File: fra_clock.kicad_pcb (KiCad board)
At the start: 2 copper layers, 210 x 297 mm, 425 parts, among them J1 USB_C, J101 SPK_TOP, J102 SPK_BOT, Q1 MMBT3904, Q2 MMBT3904, Q3 2N7002, U1 AP2112K-3.3, U101 MAX98357A, U102 MAX98357A, U2 USBLC6-2SC6, U3 ESP32-WROOM-32E, U5 CH340C, U6 74AHCT125

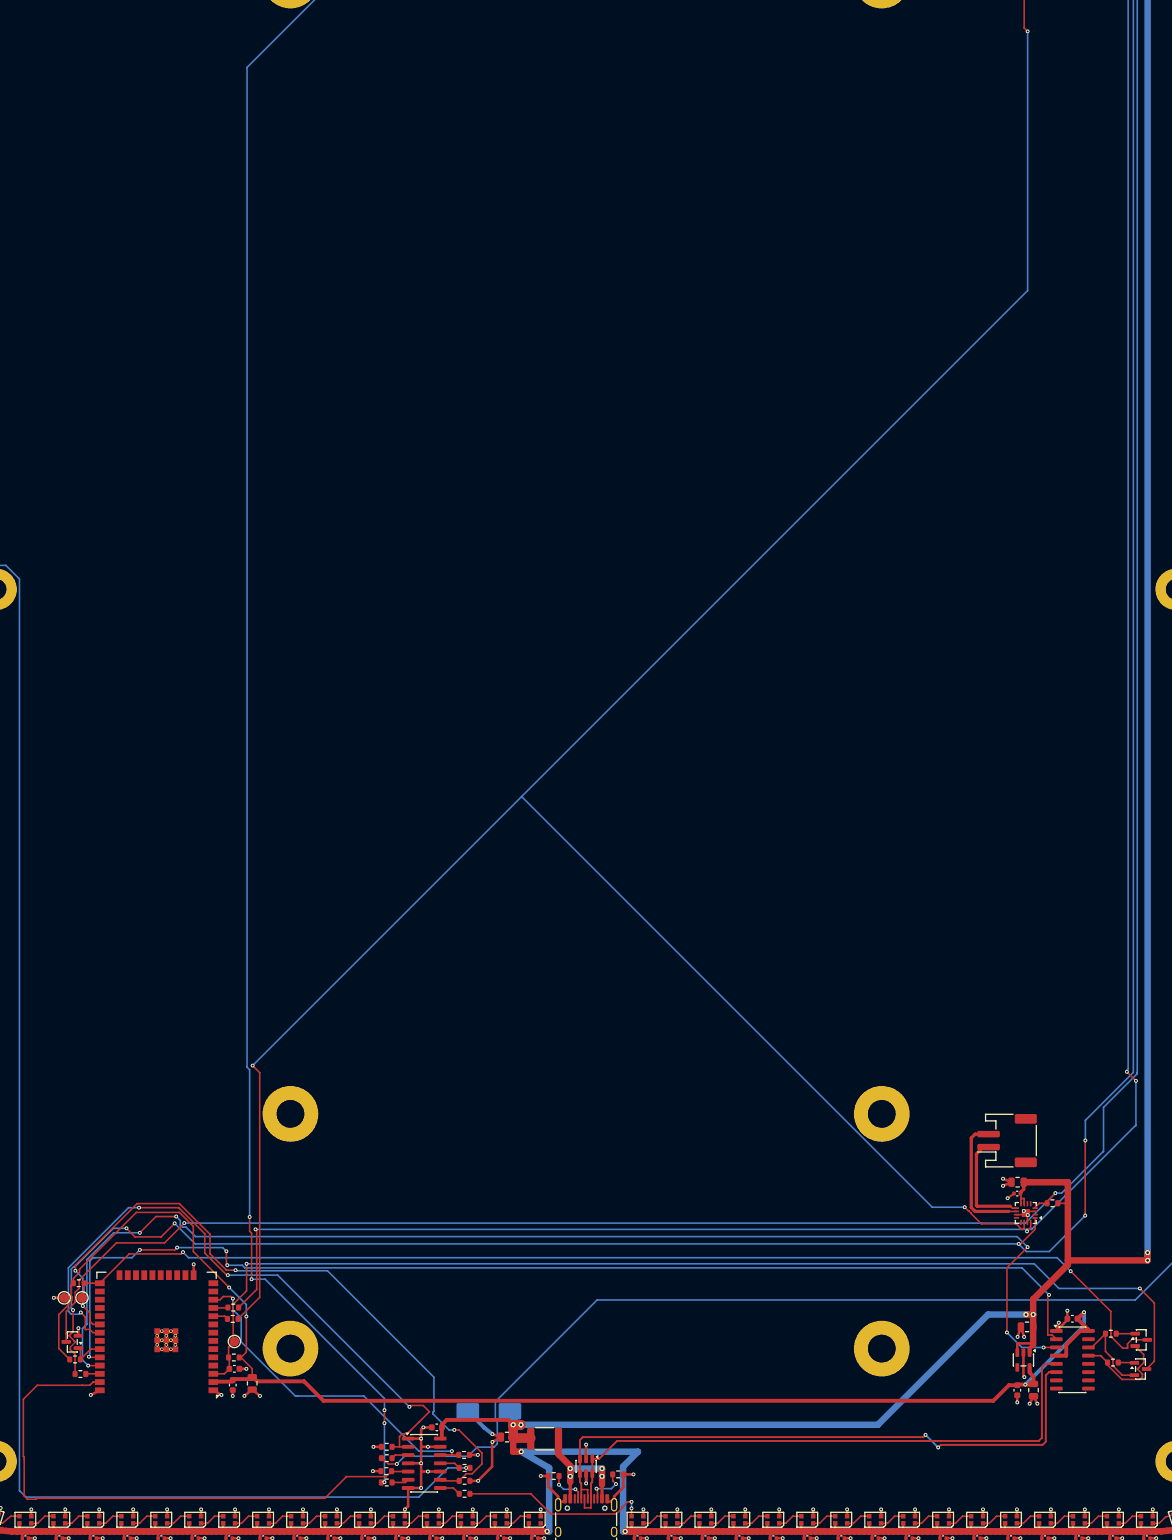
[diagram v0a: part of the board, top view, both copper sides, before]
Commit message: Art + 3D: photo footprint (F.Cu/F.Mask), Makerverse speakers on front, C69 to front east of J1, CRITICAL_AUTO regenerated
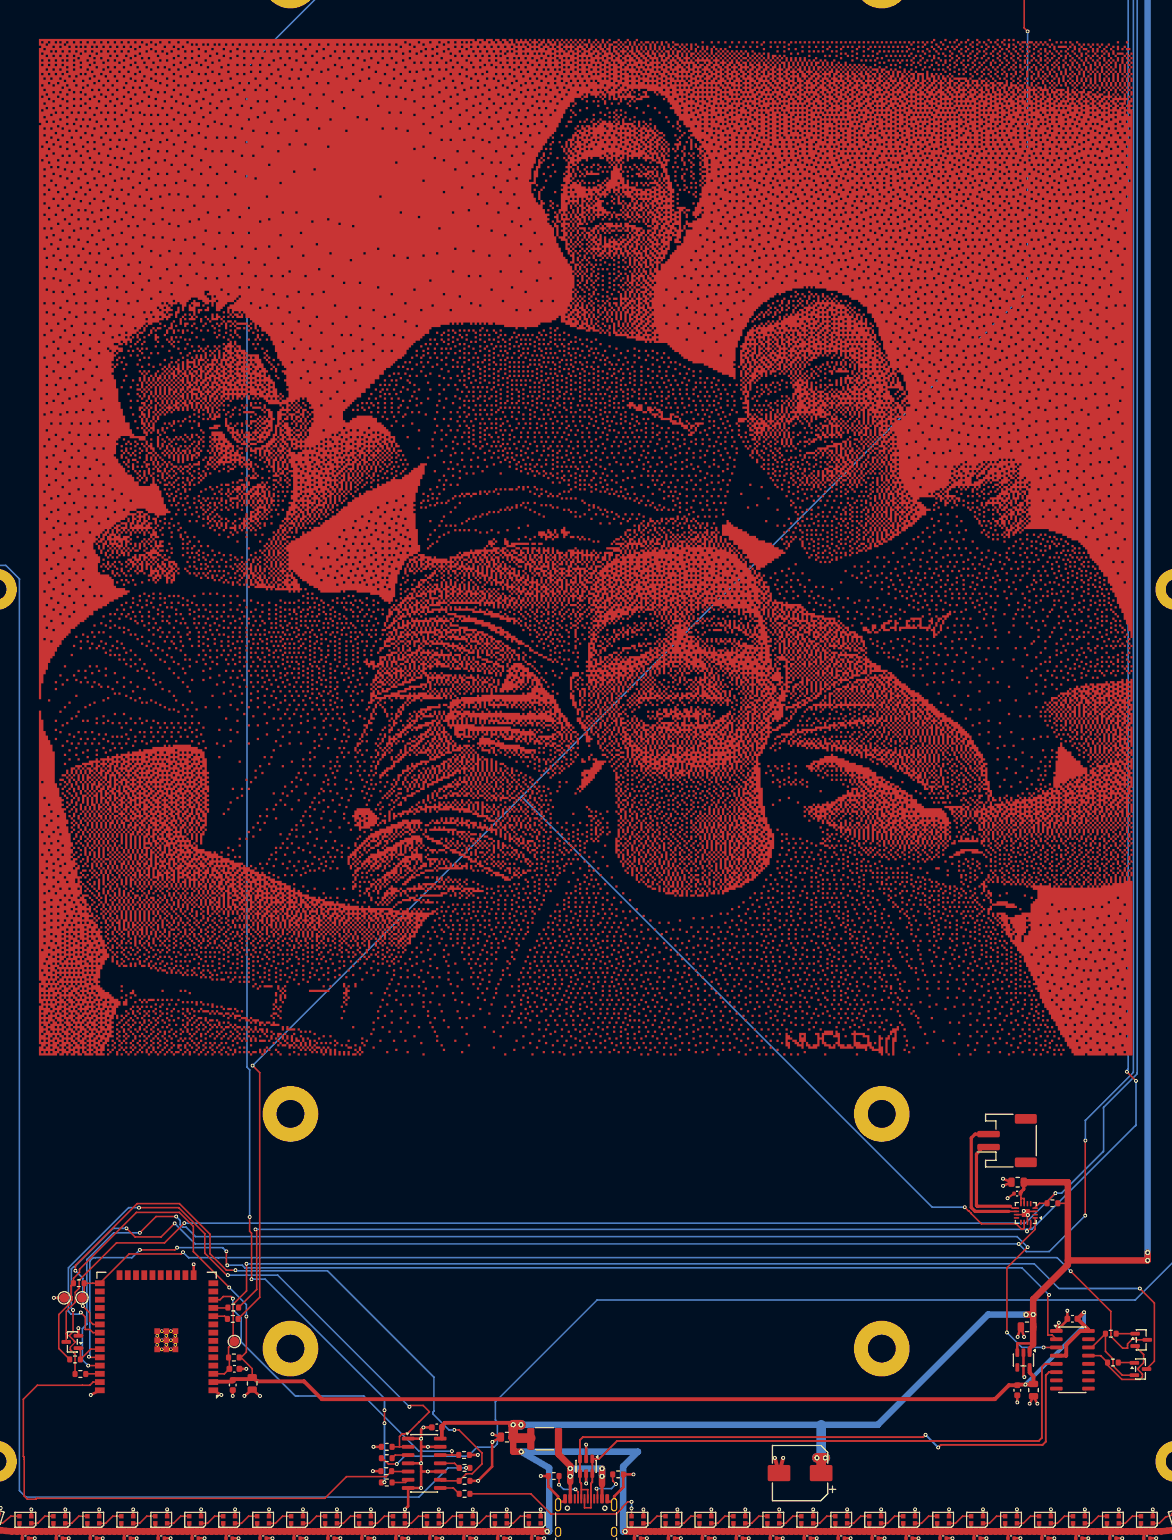
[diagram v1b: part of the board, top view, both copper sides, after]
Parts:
- added ART1: ART_FOTO, fra_clock:ART_FOTO, F.Cu at (155.0, 192.0)
- added LS1: CE08483, fra_clock:Speaker_Makerverse_CE08483_100x45, F.Cu at (155.0, 86.5)
- added LS2: CE08483, fra_clock:Speaker_Makerverse_CE08483_100x45, F.Cu at (155.0, 297.5)
- C69: moved to F.Cu
- moved C69 48.9 mm to (188.0, 334.8)
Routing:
- net +5V: track 1837.5 -> 1844.8 mm, vias 11 -> 13
- net GND: track 469.1 -> 469.9 mm, vias 402 -> 404
